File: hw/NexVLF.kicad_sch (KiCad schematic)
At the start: 36 parts, among them Q101 2N7002, Q102 2N7002, Q103 2N7002, Q104 2N7002, Q105 2N7002, U101 AK5572EN, U103 TLV9002IDDFR

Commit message: Starting some layout
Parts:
- removed U103: TLV9002IDDFR, Library:SOT95P280X145-5N, symbol Library:TLV9001IDBVR
- added C112: 1uF, Capacitor_SMD:C_0402_1005Metric, symbol Device:C
- added C113: 100nF, Capacitor_SMD:C_0402_1005Metric, symbol Device:C
- added FID101, FID102, FID103: Fiducial, Fiducial:Fiducial_0.5mm_Mask1.5mm, symbol Mechanical:Fiducial
- added H101, H102, H103, H104: MountingHole_Pad, MountingHole:MountingHole_3.2mm_M3_DIN965_Pad, symbol Mechanical:MountingHole_Pad
- added U102: TLV9001IDBVR, Library:SOT95P280X145-5N, symbol Library:TLV9001IDBVR
- renumbered C102 to C101, C103 to C102, C106 to C103, C107 to C104, C104 to C106, C108 to C107, C109 to C108, C111 to C109, C112 to C111, C303 to C114, C304 to C115, C101 to C116, C305 to C117, C306 to C118, C307 to C119, C308 to C120, C310 to C121, C311 to C122, D301 to D101, D101 to D102, R304 to R101, R104 to R102, R105 to R103, R103 to R104, R101 to R105, R102 to R106
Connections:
- net +5VA: now also C112.1, C113.1, U102.5 (V+)
- net GND: now also C112.2, C113.2, H101.1, H102.1, H103.1, H104.1, U102.2 (V-)
- net at R103.2, R105.1: now also U102.1 (OUT)
- net at C116.2, R102.1: now also U102.3 (IN+)
- net at R104.1, R105.2: now also U102.4 (IN-)
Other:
- sheet Microcontroller ports: added none; removed enable3V3
- sheet Power ports: added none; removed enable3V3
- note added: "1.667 gain: 0..3V → 0..5V"
- note removed: "1.667 gain: 0..3V --> 0..5V"

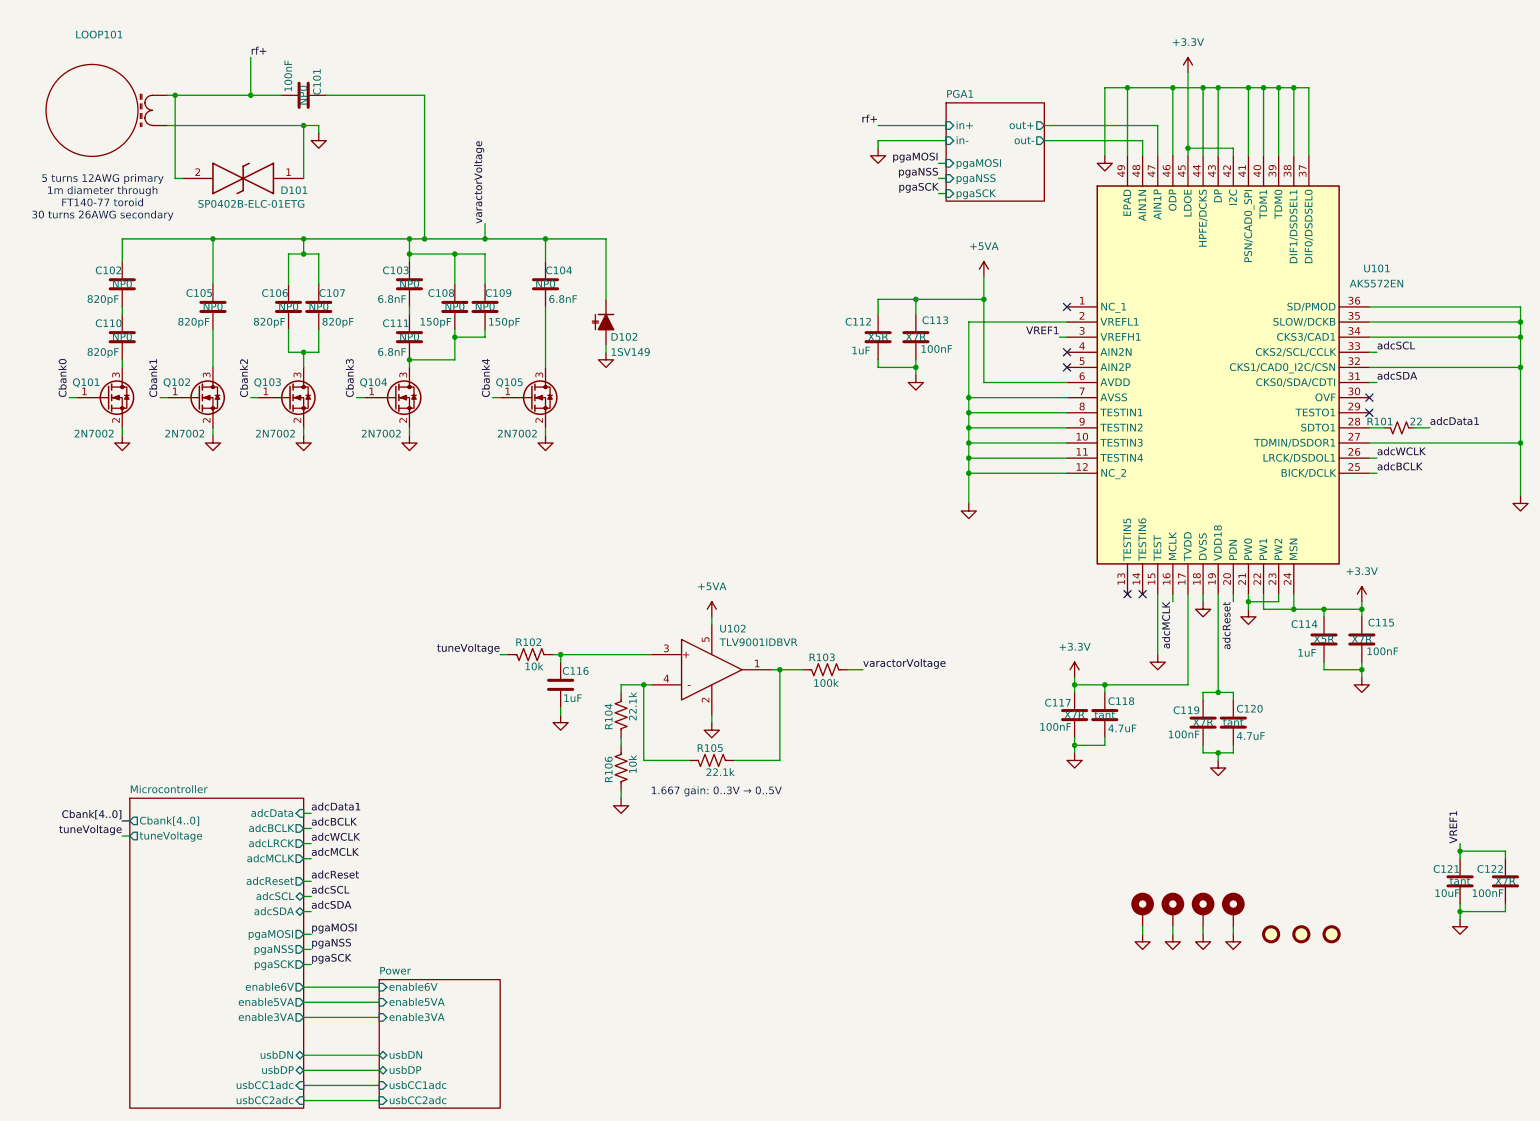
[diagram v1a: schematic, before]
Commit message: Routing complete for DVT1 all ERC and DRC pass, 3D view is full
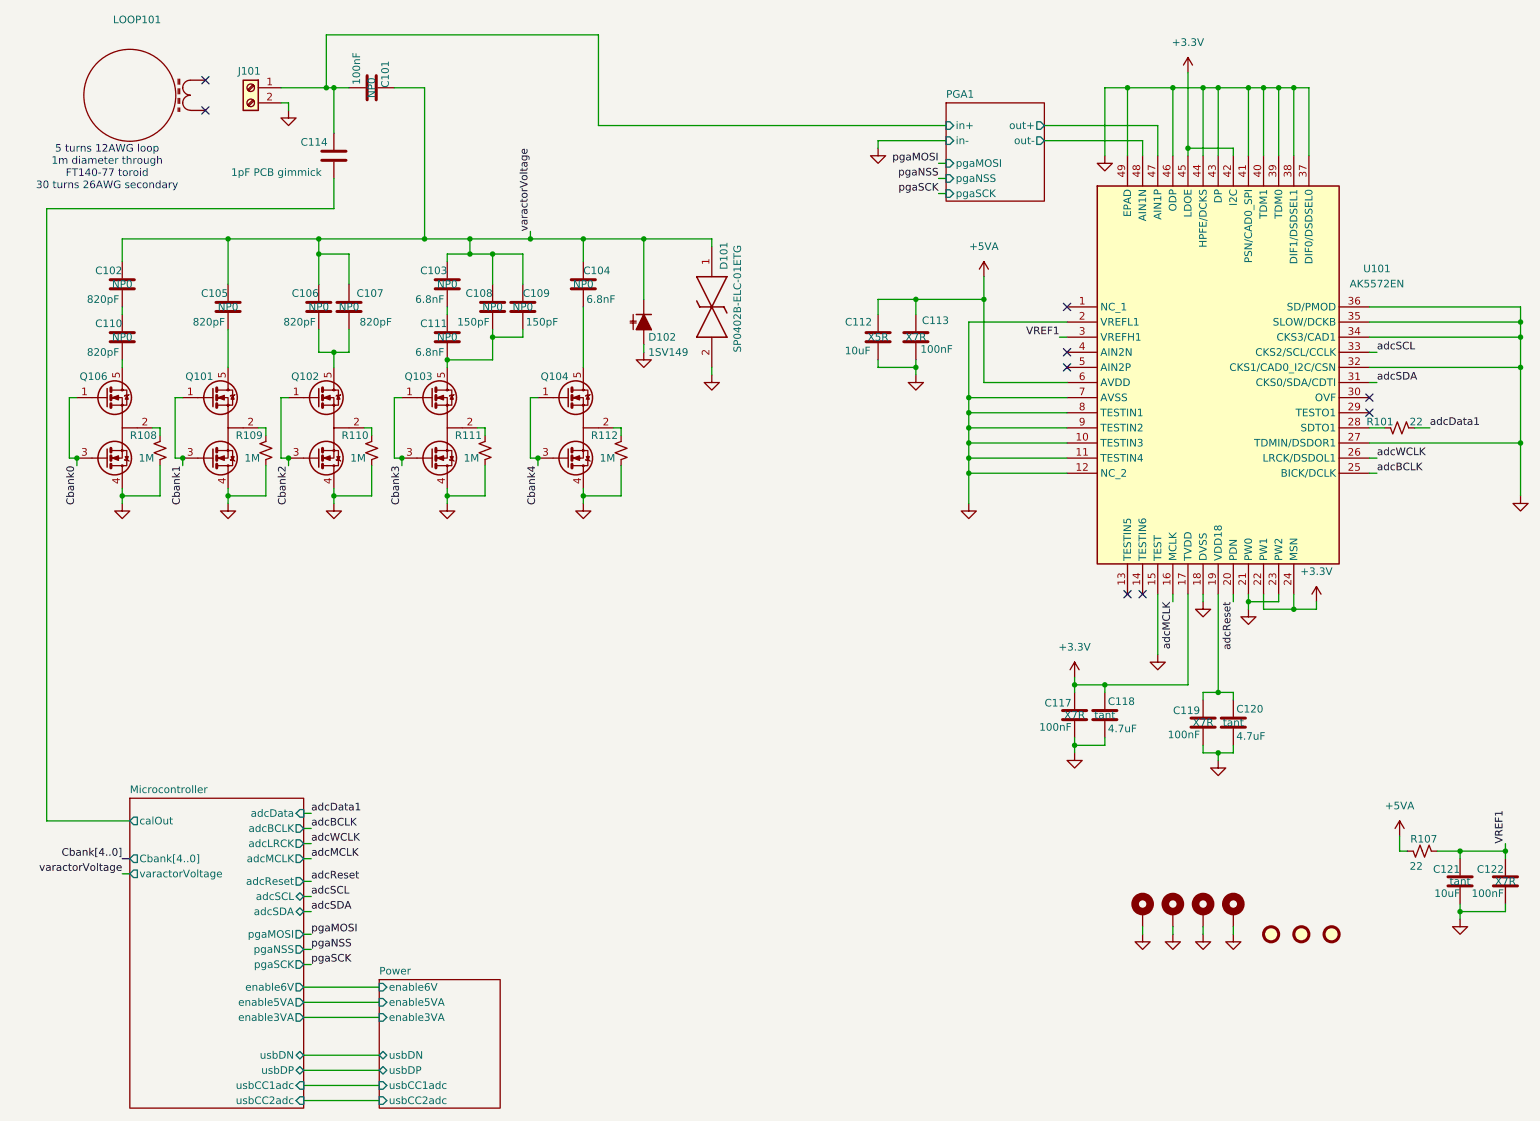
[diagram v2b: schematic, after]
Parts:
- removed C115: 100nF, Capacitor_SMD:C_0402_1005Metric, symbol Device:C
- removed C116: 1uF, Capacitor_SMD:C_0402_1005Metric, symbol Device:C
- removed Q101, Q102, Q103, Q104, Q105: 2N7002, Package_TO_SOT_SMD:SOT-23, symbol Transistor_FET:2N7002
- removed R102, R106: 10k, Resistor_SMD:R_0402_1005Metric, symbol Device:R_US
- removed R103: 100k, Resistor_SMD:R_0402_1005Metric, symbol Device:R_US
- removed R104, R105: 22.1k, Resistor_SMD:R_0402_1005Metric, symbol Device:R_US
- removed U102: TLV9001IDBVR, Library:SOT95P280X145-5N, symbol Library:TLV9001IDBVR
- added J101: ANT, TerminalBlock_Altech:Altech_AK300_1x02_P5.00mm_45-Degree, symbol Connector:Screw_Terminal_01x02
- added Q101, Q102, Q103, Q104, Q106: DMN32D2LDF, Package_TO_SOT_SMD:SOT-353_SC-70-5, symbol Transistor_FET:DMN32D2LDF
- added R107: 22, Resistor_SMD:R_0402_1005Metric, symbol Device:R_Small_US
- added R108, R109, R110, R111, R112: 1M, Resistor_SMD:R_0402_1005Metric, symbol Device:R_Small_US
- C112: value 1uF -> 10uF
- C114: value 1uF -> 1pF PCB gimmick; footprint Capacitor_SMD:C_0402_1005Metric -> Library:PCB-gimmick-1pF; LCSC_PN C301928 -> (none); MPN GRM155R61E105KE11D -> (none); Manufacturer Murata -> (none); Mouser_PN 81-GRM155R61E105KE1D -> (none); cap-type X5R -> (none); working-voltage 25V -> (none); now left out of the parts list
- D102: footprint (none) -> Package_TO_SOT_THT:TO-92-2
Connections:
- net +3.3V: no longer C114.1
- net +5VA: now also R107.2
- net Cbank0: now also Q106.1 (G1), Q106.3 (G2)
- net Cbank1: now also Q101.1 (G1), Q101.3 (G2)
- net Cbank2: now also Q102.1 (G1), Q102.3 (G2)
- net Cbank3: now also Q103.1 (G1), Q103.3 (G2)
- net Cbank4: now also Q104.1 (G1), Q104.3 (G2)
- net GND: now also D101.2, J101.2 (Pin_2), Q101.4 (D2), Q102.4 (D2), Q103.4 (D2), Q104.4 (D2), Q106.4 (D2), R108.2, R109.2, R110.2, R111.2, R112.2; no longer C114.2, D101.1, LOOP101.2 (RF2)
- net VREF1: now also R107.1
- net varactorVoltage: now also D101.1
- net at C105.2: now also Q101.5 (D1)
- net at C110.2: now also Q106.5 (D1)
- net at C106.2, C107.2: now also Q102.5 (D1)
- net at C104.2: now also Q104.5 (D1)
- net at C108.2, C109.2, C111.2: now also Q103.5 (D1)
- removed net rf+: C101.2, D101.2, LOOP101.1 (RF1)
- new net: Q103.2 (S), R111.1
- new net: Q106.2 (S), R108.1
- new net: Q104.2 (S), R112.1
- new net: Q102.2 (S), R110.1
- new net: Q101.2 (S), R109.1
- new net Microcontroller/calOut: C114.2
- new net PGA1/in+: C101.2, C114.1, J101.1 (Pin_1)
- no-connect marks 7 -> 9
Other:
- sheet Microcontroller ports: added calOut, varactorVoltage; removed tuneVoltage
- note added: "5 turns 12AWG loop 1m diameter through FT140-77 toroid 30 turns 26AWG secondary"
- note removed: "1.667 gain: 0..3V → 0..5V"
- note removed: "5 turns 12AWG primary 1m diameter through FT140-77 toroid 30 turns 26AWG secondary"
- moved on the sheet: C101, C103, C104, C105, C106, C107, C108, C109, C111, D101, D102, LOOP101
